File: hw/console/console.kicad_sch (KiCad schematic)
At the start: 155 parts, among them J1 Batt, J301 USB-C 16P, J401 DM3AT-SF-PEJM5, J501 SPK 8R, J601 FFC-40 0.5mm, J901 UART, Q601 AO3400A, SW1 Движок, SW101 UP, SW102 DOWN, SW103 LEFT, SW104 RIGHT, SW105 SELECT, SW106 START, SW107 A, SW108 B, SW109 C, SW110 D, U1 F133-A, U2 SY8089AAAC, U3 SY8089AAAC, U4 SY8089AAAC, U401 W25Q32JVSSIQ, U5 TP4056, U501 PAM8301, Y1 24 МГц, Y2 32.768 кГц

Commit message: hw: посадочные места HandSolder были стеной для веера, а сшивка портила замеры
Спросил двоих со стороны, и оба нашли то, чего я не видел.

**Стена оказалась в футпринтах.** Кольцо развязки стоит вплотную к выводам —
так и задумано, — а `C_0805_..._HandSolder` добавляет по 0.29 мм на сторону, и
вся эта прибавка приходится ровно туда, где сигналам выходить. Слева от
корпуса свободный ход был 0.40 мм у всех 32 выводов, то есть стена. Штатный
`C_0805_2012Metric` (паяем феном, `HandSolder` придуман под паяльник):
**веер выходит целиком, 90 сигналов из 90 вместо 65.**

**Замурован не только чип.** У разъёма шлейфа 26 площадок из 31 и у розетки
USB-C все 10 — тот же счёт: дорожка 0.2 с зазорами занимает 0.6 мм, при шаге
0.5 между площадками не пройти. До этих 36 площадок не дошёл бы никакой
трассировщик. Веер теперь и у них, всего 108 лучей.

**Свой трассировщик ускорен втрое** — `can_via` съедал две трети времени,
пересчитываясь для одной клетки до девяти раз, потому что направление входило
в состояние поиска. Мемоизация и состояние без направления: питание
разводится за восемь секунд вместо четырёх минут, вся плата — за минуту.

**И почему замеры плясали.** `pcb07_fanout.py` снимал дорожки, но не
переходные, а сшивка земли от прошлого круга ставится по свободному полю, то
есть каждый раз иначе. Один и тот же прогон давал то 177 несошедшихся связей,
то 206 — разница была не в том, что я правил, а в том, где вчера легли
заклёпки.

Ещё: переходная теперь занимает своё место в модели (без этого соседняя
дорожка ложилась к ней вплотную), а габарит площадки раздут на полклетки —
сетка ложится как придётся, и округление срезало до 0.025 мм зазора.

Итог: 144 неподключённых против 197, ноль нарушений DRC, прогон воспроизводим.

Трёх радиусов у веера не делаем, хотя расчёт за них: померено, с ними хуже
(195 против 177) — лучи съедают то самое место у корпуса, ради которого всё
и затевалось.

Co-Authored-By: Claude Opus 5 <noreply@anthropic.com>
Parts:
- C801, C802, C803, C804, C805, C806, C807, C808, C809, C810, C811, C812, C813, C814, C815, C816, C817, C818, C819, C820, C821, C822, C823, C824, C825, C826, C827: footprint Capacitor_SMD:C_0805_2012Metric_Pad1.18x1.45mm_HandSolder -> Capacitor_SMD:C_0805_2012Metric
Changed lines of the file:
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@@
 			)
 		)
-		(property "Footprint" "Capacitor_SMD:C_0805_2012Metric_Pad1.18x1.45mm_HandSolder"
+		(property "Footprint" "Capacitor_SMD:C_0805_2012Metric"
 			(at 236.22 290.83 0)
 			(effects
@@
 			)
 		)
-		(property "Footprint" "Capacitor_SMD:C_0805_2012Metric_Pad1.18x1.45mm_HandSolder"
+		(property "Footprint" "Capacitor_SMD:C_0805_2012Metric"
 			(at 246.38 290.83 0)
 			(effects
@@
 			)
 		)
-		(property "Footprint" "Capacitor_SMD:C_0805_2012Metric_Pad1.18x1.45mm_HandSolder"
+		(property "Footprint" "Capacitor_SMD:C_0805_2012Metric"
 			(at 256.54 290.83 0)
 			(effects
@@
 			)
 		)
-		(property "Footprint" "Capacitor_SMD:C_0805_2012Metric_Pad1.18x1.45mm_HandSolder"
+		(property "Footprint" "Capacitor_SMD:C_0805_2012Metric"
 			(at 266.7 290.83 0)
 			(effects
@@
 			)
 		)
-		(property "Footprint" "Capacitor_SMD:C_0805_2012Metric_Pad1.18x1.45mm_HandSolder"
+		(property "Footprint" "Capacitor_SMD:C_0805_2012Metric"
 			(at 276.86 290.83 0)
 			(effects
@@
 			)
 		)
-		(property "Footprint" "Capacitor_SMD:C_0805_2012Metric_Pad1.18x1.45mm_HandSolder"
+		(property "Footprint" "Capacitor_SMD:C_0805_2012Metric"
 			(at 236.22 313.69 0)
 			(effects
@@
 			)
 		)
-		(property "Footprint" "Capacitor_SMD:C_0805_2012Metric_Pad1.18x1.45mm_HandSolder"
+		(property "Footprint" "Capacitor_SMD:C_0805_2012Metric"
 			(at 246.38 313.69 0)
 			(effects
@@
 			)
 		)
-		(property "Footprint" "Capacitor_SMD:C_0805_2012Metric_Pad1.18x1.45mm_HandSolder"
+		(property "Footprint" "Capacitor_SMD:C_0805_2012Metric"
 			(at 256.54 313.69 0)
 			(effects
@@
 			)
 		)
-		(property "Footprint" "Capacitor_SMD:C_0805_2012Metric_Pad1.18x1.45mm_HandSolder"
+		(property "Footprint" "Capacitor_SMD:C_0805_2012Metric"
 			(at 266.7 313.69 0)
 			(effects
@@
 			)
 		)
-		(property "Footprint" "Capacitor_SMD:C_0805_2012Metric_Pad1.18x1.45mm_HandSolder"
+		(property "Footprint" "Capacitor_SMD:C_0805_2012Metric"
 			(at 276.86 313.69 0)
 			(effects
@@
 			)
 		)
-		(property "Footprint" "Capacitor_SMD:C_0805_2012Metric_Pad1.18x1.45mm_HandSolder"
+		(property "Footprint" "Capacitor_SMD:C_0805_2012Metric"
 			(at 287.02 313.69 0)
 			(effects
@@
 			)
 		)
-		(property "Footprint" "Capacitor_SMD:C_0805_2012Metric_Pad1.18x1.45mm_HandSolder"
+		(property "Footprint" "Capacitor_SMD:C_0805_2012Metric"
 			(at 297.18 313.69 0)
 			(effects
@@
 			)
 		)
-		(property "Footprint" "Capacitor_SMD:C_0805_2012Metric_Pad1.18x1.45mm_HandSolder"
+		(property "Footprint" "Capacitor_SMD:C_0805_2012Metric"
 			(at 236.22 337.82 0)
 			(effects
@@
 			)
 		)
-		(property "Footprint" "Capacitor_SMD:C_0805_2012Metric_Pad1.18x1.45mm_HandSolder"
+		(property "Footprint" "Capacitor_SMD:C_0805_2012Metric"
 			(at 246.38 337.82 0)
 			(effects
@@
 			)
 		)
-		(property "Footprint" "Capacitor_SMD:C_0805_2012Metric_Pad1.18x1.45mm_HandSolder"
+		(property "Footprint" "Capacitor_SMD:C_0805_2012Metric"
 			(at 256.54 337.82 0)
 			(effects
@@
 			)
 		)
-		(property "Footprint" "Capacitor_SMD:C_0805_2012Metric_Pad1.18x1.45mm_HandSolder"
+		(property "Footprint" "Capacitor_SMD:C_0805_2012Metric"
 			(at 266.7 337.82 0)
 			(effects
@@
 			)
 		)
-		(property "Footprint" "Capacitor_SMD:C_0805_2012Metric_Pad1.18x1.45mm_HandSolder"
+		(property "Footprint" "Capacitor_SMD:C_0805_2012Metric"
 			(at 276.86 337.82 0)
 			(effects
@@
 			)
 		)
-		(property "Footprint" "Capacitor_SMD:C_0805_2012Metric_Pad1.18x1.45mm_HandSolder"
+		(property "Footprint" "Capacitor_SMD:C_0805_2012Metric"
 			(at 287.02 337.82 0)
 			(effects
@@
 			)
 		)
-		(property "Footprint" "Capacitor_SMD:C_0805_2012Metric_Pad1.18x1.45mm_HandSolder"
+		(property "Footprint" "Capacitor_SMD:C_0805_2012Metric"
 			(at 287.02 290.83 0)
 			(effects
@@
 			)
 		)
-		(property "Footprint" "Capacitor_SMD:C_0805_2012Metric_Pad1.18x1.45mm_HandSolder"
+		(property "Footprint" "Capacitor_SMD:C_0805_2012Metric"
 			(at 314.96 290.83 0)
 			(effects
@@
 			)
 		)
-		(property "Footprint" "Capacitor_SMD:C_0805_2012Metric_Pad1.18x1.45mm_HandSolder"
+		(property "Footprint" "Capacitor_SMD:C_0805_2012Metric"
 			(at 327.66 290.83 0)
 			(effects
@@
 			)
 		)
-		(property "Footprint" "Capacitor_SMD:C_0805_2012Metric_Pad1.18x1.45mm_HandSolder"
+		(property "Footprint" "Capacitor_SMD:C_0805_2012Metric"
 			(at 340.36 290.83 0)
 			(effects
@@
 			)
 		)
-		(property "Footprint" "Capacitor_SMD:C_0805_2012Metric_Pad1.18x1.45mm_HandSolder"
+		(property "Footprint" "Capacitor_SMD:C_0805_2012Metric"
 			(at 307.34 325.12 0)
 			(effects
@@
 			)
 		)
-		(property "Footprint" "Capacitor_SMD:C_0805_2012Metric_Pad1.18x1.45mm_HandSolder"
+		(property "Footprint" "Capacitor_SMD:C_0805_2012Metric"
 			(at 320.04 325.12 0)
 			(effects
@@
 			)
 		)
-		(property "Footprint" "Capacitor_SMD:C_0805_2012Metric_Pad1.18x1.45mm_HandSolder"
+		(property "Footprint" "Capacitor_SMD:C_0805_2012Metric"
 			(at 332.74 325.12 0)
 			(effects
@@
 			)
 		)
-		(property "Footprint" "Capacitor_SMD:C_0805_2012Metric_Pad1.18x1.45mm_HandSolder"
+		(property "Footprint" "Capacitor_SMD:C_0805_2012Metric"
 			(at 345.44 325.12 0)
 			(effects
@@
 			)
 		)
-		(property "Footprint" "Capacitor_SMD:C_0805_2012Metric_Pad1.18x1.45mm_HandSolder"
+		(property "Footprint" "Capacitor_SMD:C_0805_2012Metric"
 			(at 358.14 325.12 0)
 			(effects

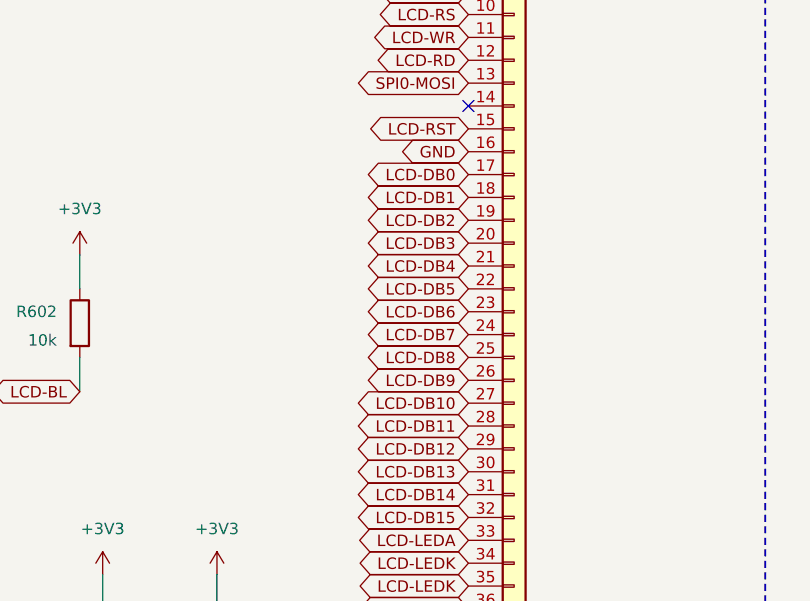
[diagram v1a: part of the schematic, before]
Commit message: hw: порядок бит на шлейфе выбран по разводке, и лучи разъёма смотрят на чип
Шина дисплея не разводилась совсем: пущенная первой по пустой плате, она
сходилась на шесть связей из тридцати шести. Разобрал до дна — оказалось три
причины, все мои.

**Лучи разъёма смотрели от чипа.** Общее правило «наружу от середины детали»
верно для корпуса с четырьмя сторонами, а у однорядного разъёма ведёт в
сторону, откуда приходит шлейф, — то есть влево, а чип справа. Вся шина
разворачивалась вокруг 26-миллиметрового корпуса. Меди под корпусом `FH12`
ничего не запрещает (зон правил у него нет, в отличие от лотка microSD), и
теперь лучи идут вправо, под корпус, прямо к чипу.

**Трассировщик целился в площадку, а не в конец луча.** Площадки мелкого шага
замурованы соседями — для того лучи и выведены, — но цель оставалась
площадкой, и лучи не помогали вовсе.

**Порядок бит был «в лоб».** Линии выходят у чипа лентой вдоль верхнего левого
угла, и при порядке по возрастанию шина обязана сама себя перекрестить в
десятимиллиметровом коридоре. Поодиночке каждая линия разводится за секунду,
вместе — не проходят. Порядок бит у нас свой: панель кормит наш же код,
перестановка вносится один раз в палитру и один раз в таблицу команд i8080.
Соответствие посчитано венгерским алгоритмом по координатам площадок:
`DB0…DB7` развёрнуты целиком, `DB10` и `DB11` поменялись местами. Шина 390 мм
и 6 пересечений вместо 415 и 13.

Ещё: кольцо развязки уступает шине горизонтальный коридор шириной по числу
линий (23 × 0.4 + запас), а конденсаторы, которым выпало это место, сдвигаются
ВДОЛЬ бока, а не уезжают за угол. Цена — четыре штуки в 7.7…12 мм от своих
выводов.

И новый шаг конвейера `pcb00_nets.py`: переносит цепи со схемы на плату из
нетлиста `kicad-cli`. Менять, какой вывод в какой цепи, — обычное проектное
решение, а «Update PCB from Schematic» живёт только в окне KiCad; без этого
каждая такая правка требовала бы ручного шага и молча ломалась бы, если про
него забыть.

Итог: неподключённых 140 против 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
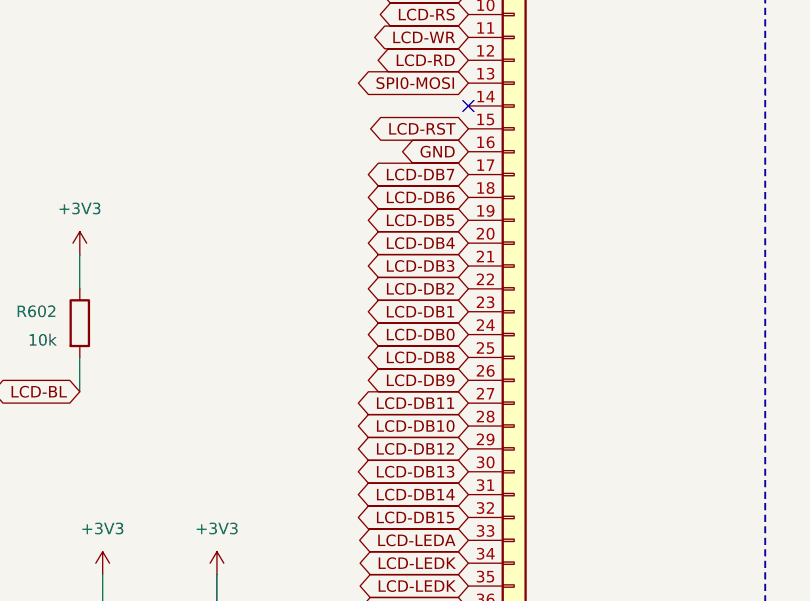
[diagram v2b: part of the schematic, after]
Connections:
- net LCD-DB0: now also J601.24 (Pin_24); no longer J601.17 (Pin_17)
- net LCD-DB1: now also J601.23 (Pin_23); no longer J601.18 (Pin_18)
- net LCD-DB10: now also J601.28 (Pin_28); no longer J601.27 (Pin_27)
- net LCD-DB11: now also J601.27 (Pin_27); no longer J601.28 (Pin_28)
- net LCD-DB2: now also J601.22 (Pin_22); no longer J601.19 (Pin_19)
- net LCD-DB3: now also J601.21 (Pin_21); no longer J601.20 (Pin_20)
- net LCD-DB4: now also J601.20 (Pin_20); no longer J601.21 (Pin_21)
- net LCD-DB5: now also J601.19 (Pin_19); no longer J601.22 (Pin_22)
- net LCD-DB6: now also J601.18 (Pin_18); no longer J601.23 (Pin_23)
- net LCD-DB7: now also J601.17 (Pin_17); no longer J601.24 (Pin_24)
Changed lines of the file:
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@@
 		(effects (font (size 1.27 1.27)) (justify right))
 	)
-	(global_label "LCD-DB0"
+	(global_label "LCD-DB7"
 		(shape bidirectional)
 		(at 541.02 278.13 180)
 		(effects (font (size 1.27 1.27)) (justify right))
 	)
-	(global_label "LCD-DB1"
+	(global_label "LCD-DB6"
 		(shape bidirectional)
 		(at 541.02 280.67 180)
 		(effects (font (size 1.27 1.27)) (justify right))
 	)
-	(global_label "LCD-DB2"
+	(global_label "LCD-DB5"
 		(shape bidirectional)
 		(at 541.02 283.21 180)
 		(effects (font (size 1.27 1.27)) (justify right))
 	)
-	(global_label "LCD-DB3"
+	(global_label "LCD-DB4"
 		(shape bidirectional)
 		(at 541.02 285.75 180)
 		(effects (font (size 1.27 1.27)) (justify right))
 	)
-	(global_label "LCD-DB4"
+	(global_label "LCD-DB3"
 		(shape bidirectional)
 		(at 541.02 288.29 180)
 		(effects (font (size 1.27 1.27)) (justify right))
 	)
-	(global_label "LCD-DB5"
+	(global_label "LCD-DB2"
 		(shape bidirectional)
 		(at 541.02 290.83 180)
 		(effects (font (size 1.27 1.27)) (justify right))
 	)
-	(global_label "LCD-DB6"
+	(global_label "LCD-DB1"
 		(shape bidirectional)
 		(at 541.02 293.37 180)
 		(effects (font (size 1.27 1.27)) (justify right))
 	)
-	(global_label "LCD-DB7"
+	(global_label "LCD-DB0"
 		(shape bidirectional)
 		(at 541.02 295.91 180)
@@
 		(effects (font (size 1.27 1.27)) (justify right))
 	)
-	(global_label "LCD-DB10"
+	(global_label "LCD-DB11"
 		(shape bidirectional)
 		(at 541.02 303.53 180)
 		(effects (font (size 1.27 1.27)) (justify right))
 	)
-	(global_label "LCD-DB11"
+	(global_label "LCD-DB10"
 		(shape bidirectional)
 		(at 541.02 306.07 180)

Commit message: hw: между дорожками требовалось 0.6 мм вместо 0.4 — шина проходила через одну
Раздутие площадки и раздутие дорожки — разные величины, а в модели занятости
стояла одна на обе. У площадки раздувается край: от края до чужой оси нужен
зазор плюс полдорожки, 0.3 мм, две клетки. У дорожки раздувается ось: от оси
до оси нужно полдорожки плюс зазор плюс полдорожки, ровно 0.4 мм — тоже две
клетки, но «закрыто две клетки» означает, что чужая ось встанет только на
третьей. Ошибка в одну клетку, полуторный шаг.

Шина дисплея идёт с минимальным шагом 0.4, и это её убивало. Померено на
пустой плате, где мешать некому: 4 линии данных из 16, и проходили они
через одну.

Порядок бит на шлейфе был выбран венгерским алгоритмом по расстояниям — то
есть минимизацией длины, тогда как решают пересечения. На этой шине два
критерия дают противоположные ответы: минимум длины разворачивает DB0..DB7
целиком. Правильный признак — порядок обхода: выводы шлейфа сверху вниз,
выводы чипа от «кому дальше огибать угол» к «кому ближе». Получается почти
прямой порядок; единственная перестановка не наша, а корпуса — PD12 и PD13
стоят в eLQFP не по порядку.

Таблица 06-display.md §2.8 держала строки 27 и 28 в обратном порядке, то есть
прописывала шине перекрёст в этом самом месте. Правлен документ, код был прав.

Кнопки поменяны сторонами: крестовина сидела на выводах 1..4, смотрящих
вправо, а стоит у левого края платы; A..D сидели на 124..127, смотрящих вниз,
а стоят справа. Две группы шли навстречу и пересекались на ровном месте.
Перестановка бесплатная — PG6..PG15 неотличимы по §2.1, — и резерв PG0..PG5
под SDC1 не тронут.

Трассировщик получил два новых понятия: закреплённый коридор (чужой цепи вход
платный) и ленту (пучок кладётся подряд и по порядку обхода, а не вперемешку
по длине).

Co-Authored-By: Claude Opus 5 <noreply@anthropic.com>
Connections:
- net KEY-A: now also U1.2 (PG7); no longer U1.124 (PG12)
- net KEY-B: now also U1.3 (PG8); no longer U1.125 (PG13)
- net KEY-C: now also U1.1 (PG6); no longer U1.126 (PG14)
- net KEY-D: now also U1.4 (PG9); no longer U1.127 (PG15)
- net KEY-DOWN: now also U1.125 (PG13); no longer U1.2 (PG7)
- net KEY-LEFT: now also U1.126 (PG14); no longer U1.3 (PG8)
- net KEY-RIGHT: now also U1.127 (PG15); no longer U1.4 (PG9)
- net KEY-UP: now also U1.124 (PG12); no longer U1.1 (PG6)
- net LCD-DB0: now also J601.17 (Pin_17); no longer J601.24 (Pin_24)
- net LCD-DB1: now also J601.18 (Pin_18); no longer J601.23 (Pin_23)
- net LCD-DB2: now also J601.19 (Pin_19); no longer J601.22 (Pin_22)
- net LCD-DB3: now also J601.20 (Pin_20); no longer J601.21 (Pin_21)
- net LCD-DB4: now also J601.21 (Pin_21); no longer J601.20 (Pin_20)
- net LCD-DB5: now also J601.22 (Pin_22); no longer J601.19 (Pin_19)
- net LCD-DB6: now also J601.23 (Pin_23); no longer J601.18 (Pin_18)
- net LCD-DB7: now also J601.24 (Pin_24); no longer J601.17 (Pin_17)
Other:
- note added: "выводы PG6..PG15 (1..6 и 124..127)"
- note added: "кто на каком — выбрано разводкой, см. блок 8"
- note removed: "верхний ряд: PG6..PG11, выводы 1..6"
- note removed: "нижний ряд: PG12..PG15, выводы 124..127"

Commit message: hw: гребёнки на торце — угловые, и pcb00_sync больше не падает на полпути
Три гребёнки J1, J501, J901 стоят на нижнем торце платы, и смысл у них
один: провод наружу. Вертикальная торчит на 8.5 мм и уводит провод
вверх, под стекло, где просвет 2.0. В схеме стояли вертикальные
посадочные места — схема противоречила механике. Нашёл это чужой агент,
описывавший деталь по нашим документам, а не я.

pcb00_sync при этом упал на втором корпусе из трёх: FootprintLoad после
первого board.Remove падает с «SwigPyObject has no attribute
FootprintLoad» — pcbnew портит объект плагина так же, как портит
контейнер корпусов. Это ровно те грабли, про которые написано в шапке
самого файла, только на другом объекте. Теперь всё из библиотеки
читается заранее, а сверка нумерации идёт ДО подмены: корпус, который
подменяет sync, приходит из библиотеки с правильной нумерацией по
построению.

Схема перерисована, ERC 0, audit 0. DRC по меди чист. Разрывов 130,
столько же, сколько до замены.

Co-Authored-By: Claude Opus 5 <noreply@anthropic.com>
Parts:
- J1, J501: footprint Connector_PinHeader_2.54mm:PinHeader_1x02_P2.54mm_Vertical -> Connector_PinHeader_2.54mm:PinHeader_1x02_P2.54mm_Horizontal
- J901: footprint Connector_PinHeader_2.54mm:PinHeader_1x04_P2.54mm_Vertical -> Connector_PinHeader_2.54mm:PinHeader_1x04_P2.54mm_Horizontal

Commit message: hw: место в кольце развязки выбирает расстояние, а не правило
Выбор «ряд наружу или сдвиг вдоль бока» делало правило: сперва ближний
ряд при любом сдвиге вдоль, до десяти миллиметров, и только потом ряд
дальше. Правило звучало разумно и на малых сдвигах верно, а на больших
врёт вдвое: третий ряд уводит от вывода на 2.5 мм, сдвиг вдоль — на все
десять. Так C801 уехал за угол корпуса и встал в 16.6 мм от вывода 83,
при том что место в третьем ряду напротив вывода было свободно.

Теперь из всех свободных мест берётся ближайшее к своему выводу — это
единственная честная мера, смысл развязки в короткой петле тока.
Третий ряд разрешён: он перестал быть поблажкой, стал ещё одним местом
на выбор.

Замер: связей 138 -> 147, разрывов 130 -> 126, худшая ёмкость 16.6 ->
12.0 мм. Ёмкостей дальше 7 мм стало 11 против 9 — это цена, и она
принята: ёмкость в 16 мм не развязывает вовсе, а 8 вместо 7 работает
хуже, но работает.

Заодно три дефекта в самом кольце:

Кольцо не смотрело на чужие корпуса, только на запреты. Пока выбор был
жадным, до чужих деталей дело не доходило; по расстоянию C802 сразу
село на TP801.

Проверка занятости меряла корпус НЕПОВЁРНУТЫМ: у верхней и нижней
сторон деталь ставится на 90°, а ширина с высотой не менялись. У боков
совпадало случайно, у верха и низа врало.

Ветка «места нет» ставила деталь молча и без всякой проверки. Теперь
она говорит: шести ёмкостям (выводы 77, 81, 83, 89) места в кольце нет
вовсе — левый бок занят разъёмом шлейфа и коридором шины.

Уход на соседнюю сторону пробовали и отказались: средняя 6.8 -> 8.3 мм,
худшая 12.0 -> 19.1. За углом свободно как раз то, что дальше всего от
вывода.

Гребёнки возвращены на ВЕРТИКАЛЬНЫЕ. Мой прошлый вывод «угловые» был
неверен, и поймала это проверка платы: J901 залез под панель на 2.7 мм.
Габариты из библиотеки: угловая 1x04 занимает вглубь 12.3 мм,
вертикальная 3.5, полоса вне габарита панели 9.7. Угловая не влезает.
А 8.5 мм у вертикальной законны: просвет 2.0 действует ПОД панелью, а
гребёнки ст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
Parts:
- J1, J501: footprint Connector_PinHeader_2.54mm:PinHeader_1x02_P2.54mm_Horizontal -> Connector_PinHeader_2.54mm:PinHeader_1x02_P2.54mm_Vertical
- J901: footprint Connector_PinHeader_2.54mm:PinHeader_1x04_P2.54mm_Horizontal -> Connector_PinHeader_2.54mm:PinHeader_1x04_P2.54mm_Vertical
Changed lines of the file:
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@@
 			)
 		)
-		(property "Footprint" "Connector_PinHeader_2.54mm:PinHeader_1x02_P2.54mm_Horizontal"
+		(property "Footprint" "Connector_PinHeader_2.54mm:PinHeader_1x02_P2.54mm_Vertical"
 			(at 426.72 43.18 0)
 			(effects
@@
 			)
 		)
-		(property "Footprint" "Connector_PinHeader_2.54mm:PinHeader_1x02_P2.54mm_Horizontal"
+		(property "Footprint" "Connector_PinHeader_2.54mm:PinHeader_1x02_P2.54mm_Vertical"
 			(at 490.22 170.18 0)
 			(effects
@@
 			)
 		)
-		(property "Footprint" "Connector_PinHeader_2.54mm:PinHeader_1x04_P2.54mm_Horizontal"
+		(property "Footprint" "Connector_PinHeader_2.54mm:PinHeader_1x04_P2.54mm_Vertical"
 			(at 76.2 365.76 0)
 			(effects
